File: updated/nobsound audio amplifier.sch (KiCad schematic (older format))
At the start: 0 parts

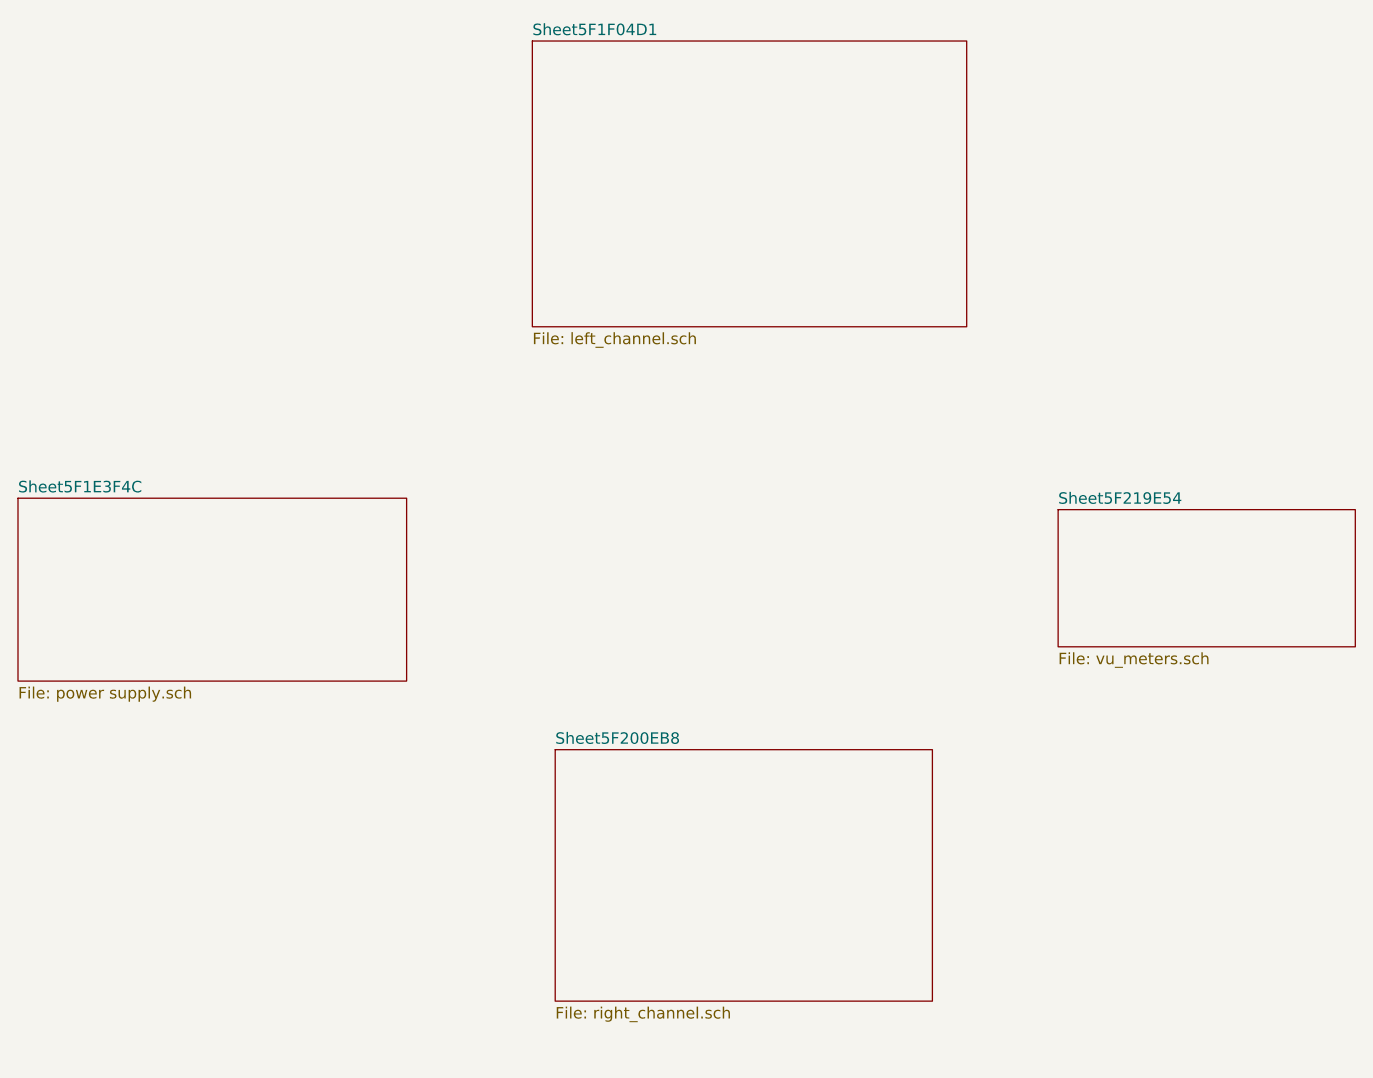
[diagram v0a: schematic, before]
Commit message: adding some components to try to stop a high pitch squal sound I sometimes hear from the amp
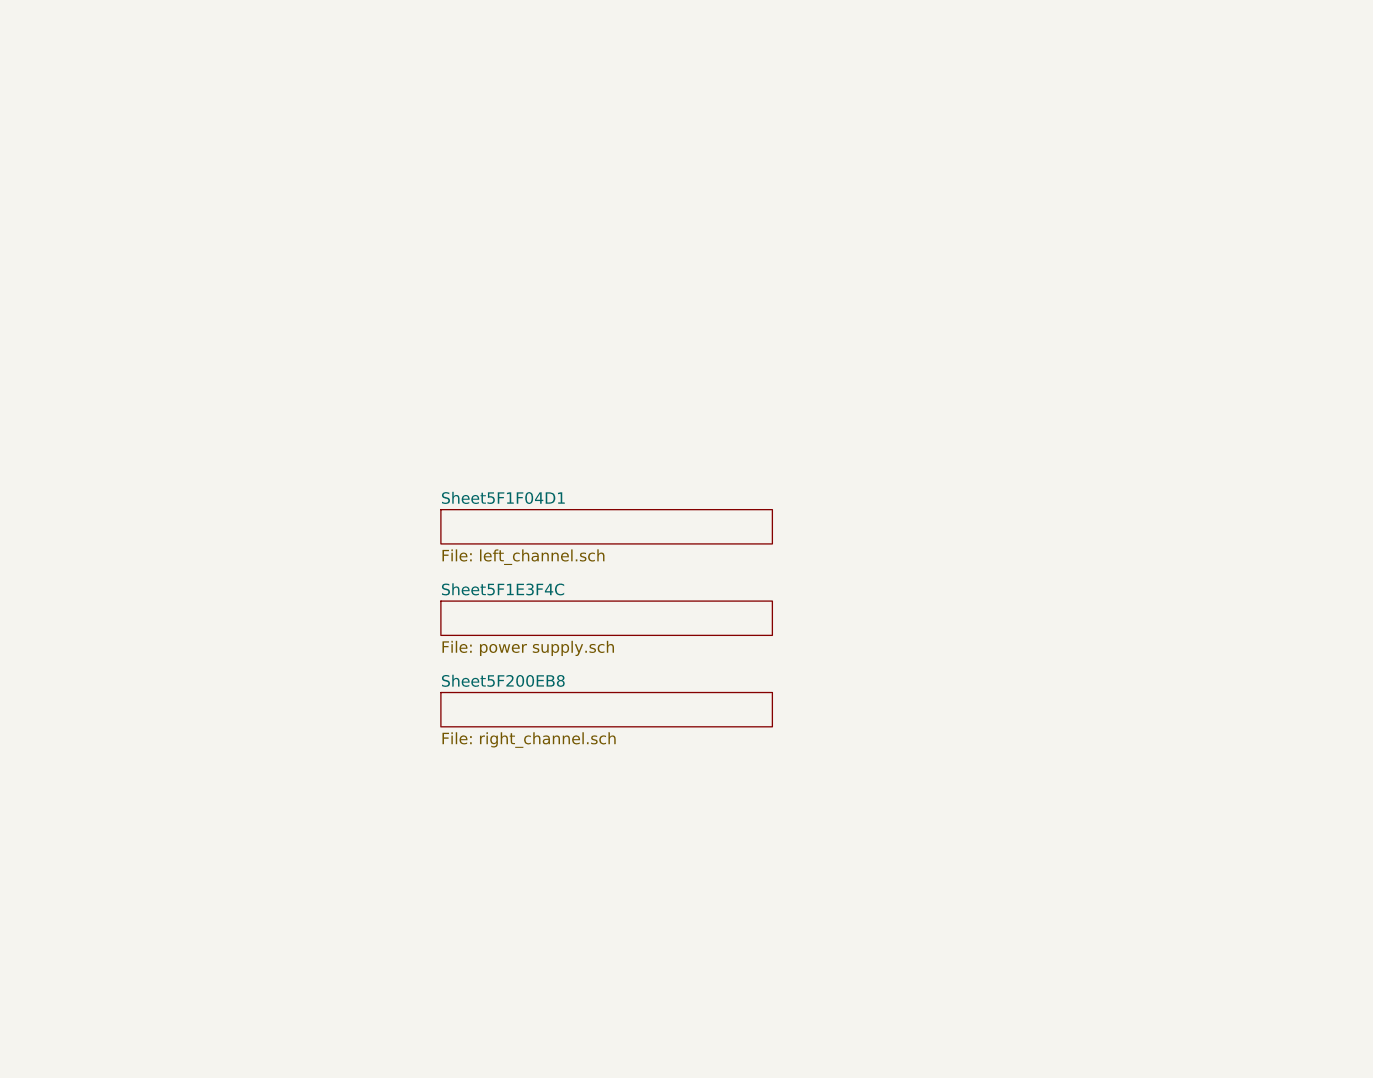
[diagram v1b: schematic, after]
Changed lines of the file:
@@
 $Descr A4 11693 8268
 encoding utf-8
-Sheet 1 5
+Sheet 1 4
 Title ""
 Date ""
@@
 $EndDescr
 $Sheet
-S 2700 3050 1700 800
+S 4550 3500 1450 150
 U 5F1E3F4D
 F0 "Sheet5F1E3F4C" 50
@@
 $EndSheet
 $Sheet
-S 4950 1050 1900 1250
+S 4550 3100 1450 150
 U 5F1F04D2
 F0 "Sheet5F1F04D1" 50
@@
 $EndSheet
 $Sheet
-S 5050 4150 1650 1100
+S 4550 3900 1450 150
 U 5F200EB9
 F0 "Sheet5F200EB8" 50
 F1 "right_channel.sch" 50
 $EndSheet
-$Sheet
-S 7250 3100 1300 600
-U 5F219E55
-F0 "Sheet5F219E54" 50
-F1 "vu_meters.sch" 50
-$EndSheet
 $EndSCHEMATC

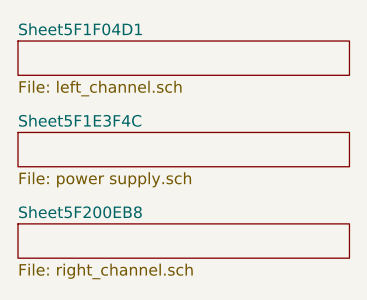
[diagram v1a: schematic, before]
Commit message: update schematic
Replaced all the counterfeit capacitor between preamp and power stage. Really opened up the sound.
Add some pictures
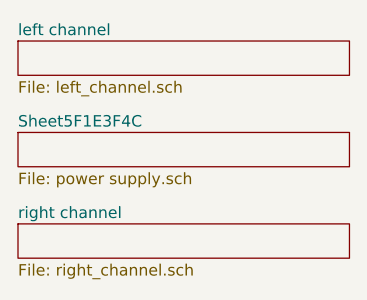
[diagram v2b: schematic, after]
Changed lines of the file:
@@
 S 4550 3100 1450 150
 U 5F1F04D2
-F0 "Sheet5F1F04D1" 50
+F0 "left channel" 50
 F1 "left_channel.sch" 50
 $EndSheet
@@
 S 4550 3900 1450 150
 U 5F200EB9
-F0 "Sheet5F200EB8" 50
+F0 "right channel" 50
 F1 "right_channel.sch" 50
 $EndSheet

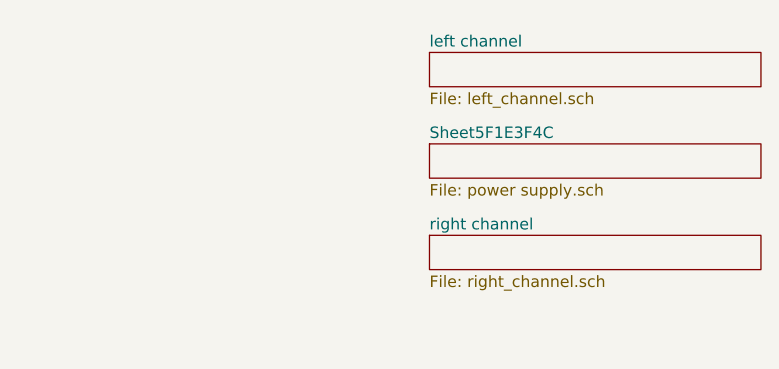
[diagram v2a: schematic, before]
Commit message: It didn't sound right to me
I don't understand how changing the cathode bypass a bit made the amp a lot more brighter. Theory is the power supply was over loaded before and it was not able to drive the high frequency things out?
Changed more capacitors. Added  plate bypass cap to preamp.
Sounds much better now.
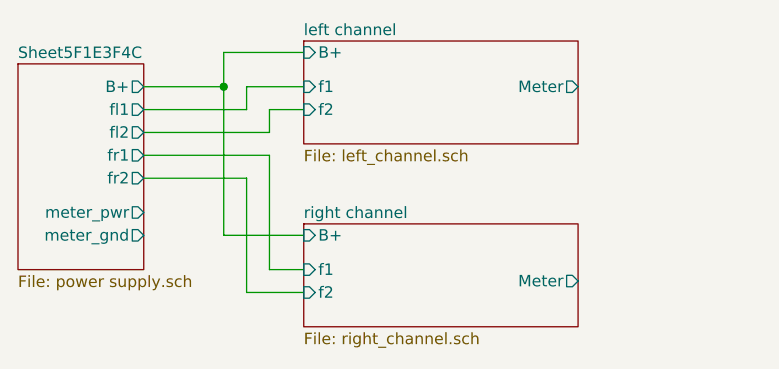
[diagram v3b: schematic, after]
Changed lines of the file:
@@
 $EndDescr
 $Sheet
-S 4550 3500 1450 150
+S 2750 3150 550  900
 U 5F1E3F4D
 F0 "Sheet5F1E3F4C" 50
 F1 "power supply.sch" 50
+F2 "B+" O R 3300 3250 50
+F3 "fl1" O R 3300 3350 50
+F4 "fl2" O R 3300 3450 50
+F5 "fr1" O R 3300 3550 50
+F6 "fr2" O R 3300 3650 50
+F7 "meter_pwr" O R 3300 3800 50
+F8 "meter_gnd" O R 3300 3900 50
 $EndSheet
 $Sheet
-S 4550 3100 1450 150
+S 4000 3050 1200 450
 U 5F1F04D2
 F0 "left channel" 50
 F1 "left_channel.sch" 50
+F2 "B+" I L 4000 3100 50
+F3 "Meter" O R 5200 3250 50
+F4 "f1" I L 4000 3250 50
+F5 "f2" I L 4000 3350 50
 $EndSheet
 $Sheet
-S 4550 3900 1450 150
+S 4000 3850 1200 450
 U 5F200EB9
 F0 "right channel" 50
 F1 "right_channel.sch" 50
+F2 "Meter" O R 5200 4100 50
+F3 "B+" I L 4000 3900 50
+F4 "f1" I L 4000 4050 50
+F5 "f2" I L 4000 4150 50
 $EndSheet
+Wire Wire Line
+	3300 3250 3650 3250
+Wire Wire Line
+	3650 3250 3650 3100
+Wire Wire Line
+	3650 3100 4000 3100
+Wire Wire Line
+	4000 3900 3650 3900
+Wire Wire Line
+	3650 3900 3650 3250
+Connection ~ 3650 3250
+Wire Wire Line
+	4000 3250 3750 3250
+Wire Wire Line
+	3750 3250 3750 3350
+Wire Wire Line
+	3750 3350 3300 3350
+Wire Wire Line
+	4000 3350 3850 3350
+Wire Wire Line
+	3850 3450 3300 3450
+Wire Wire Line
+	3850 3350 3850 3450
+Wire Wire Line
+	3300 3550 3850 3550
+Wire Wire Line
+	3850 3550 3850 4050
+Wire Wire Line
+	3850 4050 4000 4050
+Wire Wire Line
+	4000 4150 3750 4150
+Wire Wire Line
+	3750 4150 3750 3650
+Wire Wire Line
+	3750 3650 3300 3650
 $EndSCHEMATC

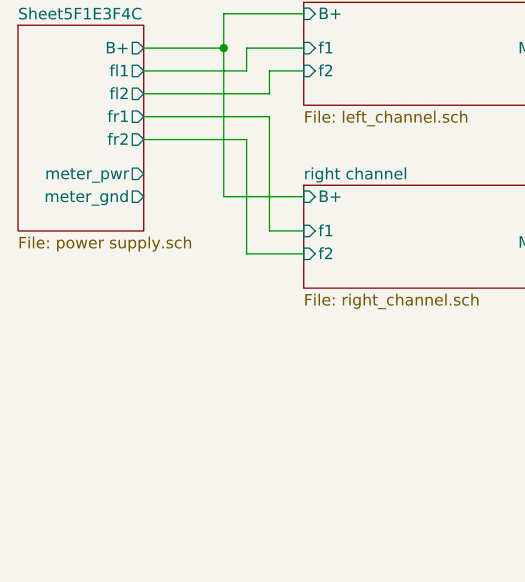
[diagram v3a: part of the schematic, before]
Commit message: v2.5 modifications
fix the audio bleedthrough, add soft suspend switch
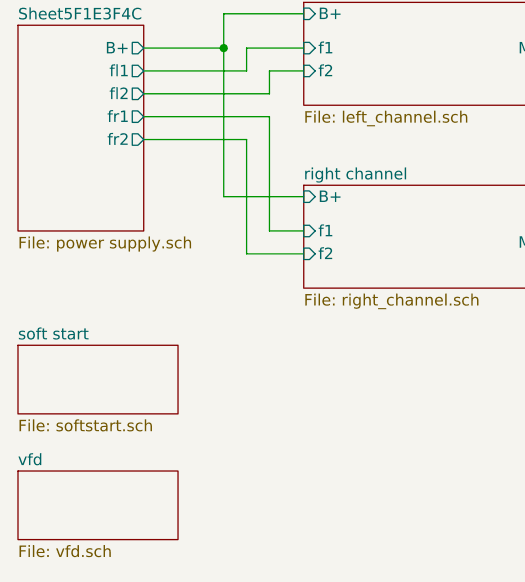
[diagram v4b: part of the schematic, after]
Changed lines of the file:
@@
 $Descr A4 11693 8268
 encoding utf-8
-Sheet 1 4
+Sheet 1 6
 Title ""
 Date ""
@@
 Comment4 ""
 $EndDescr
-$Sheet
-S 2750 3150 550  900
-U 5F1E3F4D
-F0 "Sheet5F1E3F4C" 50
-F1 "power supply.sch" 50
-F2 "B+" O R 3300 3250 50
-F3 "fl1" O R 3300 3350 50
-F4 "fl2" O R 3300 3450 50
-F5 "fr1" O R 3300 3550 50
-F6 "fr2" O R 3300 3650 50
-F7 "meter_pwr" O R 3300 3800 50
-F8 "meter_gnd" O R 3300 3900 50
-$EndSheet
 $Sheet
 S 4000 3050 1200 450
@@
 Wire Wire Line
 	3750 3650 3300 3650
+$Sheet
+S 2750 5100 700  300
+U 60AEF536
+F0 "vfd" 50
+F1 "vfd.sch" 50
+$EndSheet
+$Sheet
+S 2750 4550 700  300
+U 60B94563
+F0 "soft start" 50
+F1 "softstart.sch" 50
+$EndSheet
+$Sheet
+S 2750 3150 550  900
+U 5F1E3F4D
+F0 "Sheet5F1E3F4C" 50
+F1 "power supply.sch" 50
+F2 "B+" O R 3300 3250 50
+F3 "fl1" O R 3300 3350 50
+F4 "fl2" O R 3300 3450 50
+F5 "fr1" O R 3300 3550 50
+F6 "fr2" O R 3300 3650 50
+$EndSheet
 $EndSCHEMATC
